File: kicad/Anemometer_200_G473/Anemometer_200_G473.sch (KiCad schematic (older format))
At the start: 81 parts, among them J1 Conn_01x01_Female, J10 Conn_01x01_Female, J11 USB_B_Micro, J12 Conn_01x01_Female, J13 Conn_01x01_Female, J14 Conn_01x01_Female, J15 Conn_01x01_Female, J16 Conn_01x01_Female, J17 Conn_01x01_Female, J18 Conn_01x01_Female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

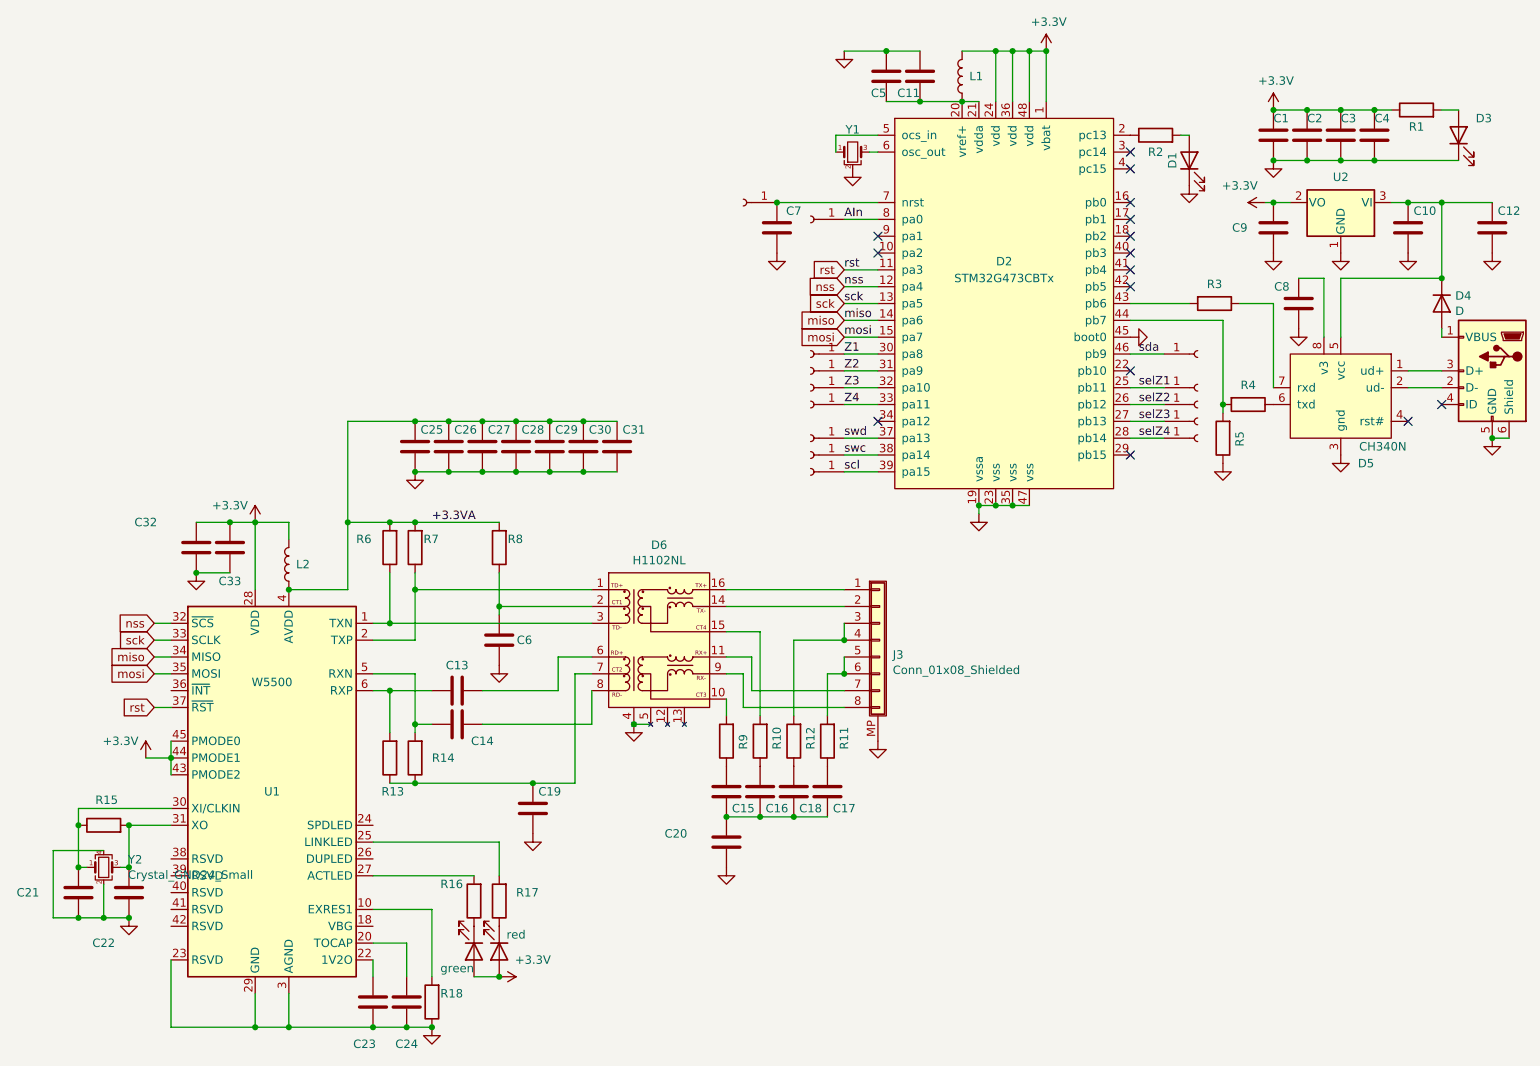
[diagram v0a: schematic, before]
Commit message: изменено:      kicad/Anemometer_200_G473/Anemometer_200_G473-cache.lib 	изменено:      kicad/Anemometer_200_G473/Anemometer_200_G473.kicad_pcb 	изменено:      kicad/Anemometer_200_G473/Anemometer_200_G473.kicad_pcb-bak 	изменено:      kicad/Anemometer_200_G473/Anemometer_200_G473.sch 	изменено:      kicad/Anemometer_200_G473/Anemometer_200_G473.sch-bak 	изменено:      kicad/Anemometer_200_G473/sym-lib-table 	изменено:      stm32cubeide/Anemometer_G474CBT6_MATLAB/Anemometer_G473CBT7_MATLAB.ioc 	изменено:      stm32cubeide/Anemometer_G474CBT6_MATLAB/Core/Inc/main.h 	изменено:      stm32cubeide/Anemometer_G474CBT6_MATLAB/Core/Src/main.c 	изменено:      stm32cubeide/Anemometer_G474CBT6_MATLAB/Release/Anemometer_G473CBT7_MATLAB.elf 	изменено:      stm32cubeide/Anemometer_G474CBT6_MATLAB/Release/Anemometer_G473CBT7_MATLAB.list 	изменено:      stm32cubeide/Anemometer_G474CBT6_MATLAB/Release/Anemometer_G473CBT7_MATLAB.map 	изменено:      stm32cubeide/Anemometer_G474CBT6_MATLAB/Release/Core/Src/main.cyclo 	изменено:      stm32cubeide/Anemometer_G474CBT6_MATLAB/Release/Core/Src/main.o 	изменено:      stm32cubeide/Anemometer_G474CBT6_MATLAB/Release/Core/Src/main.su
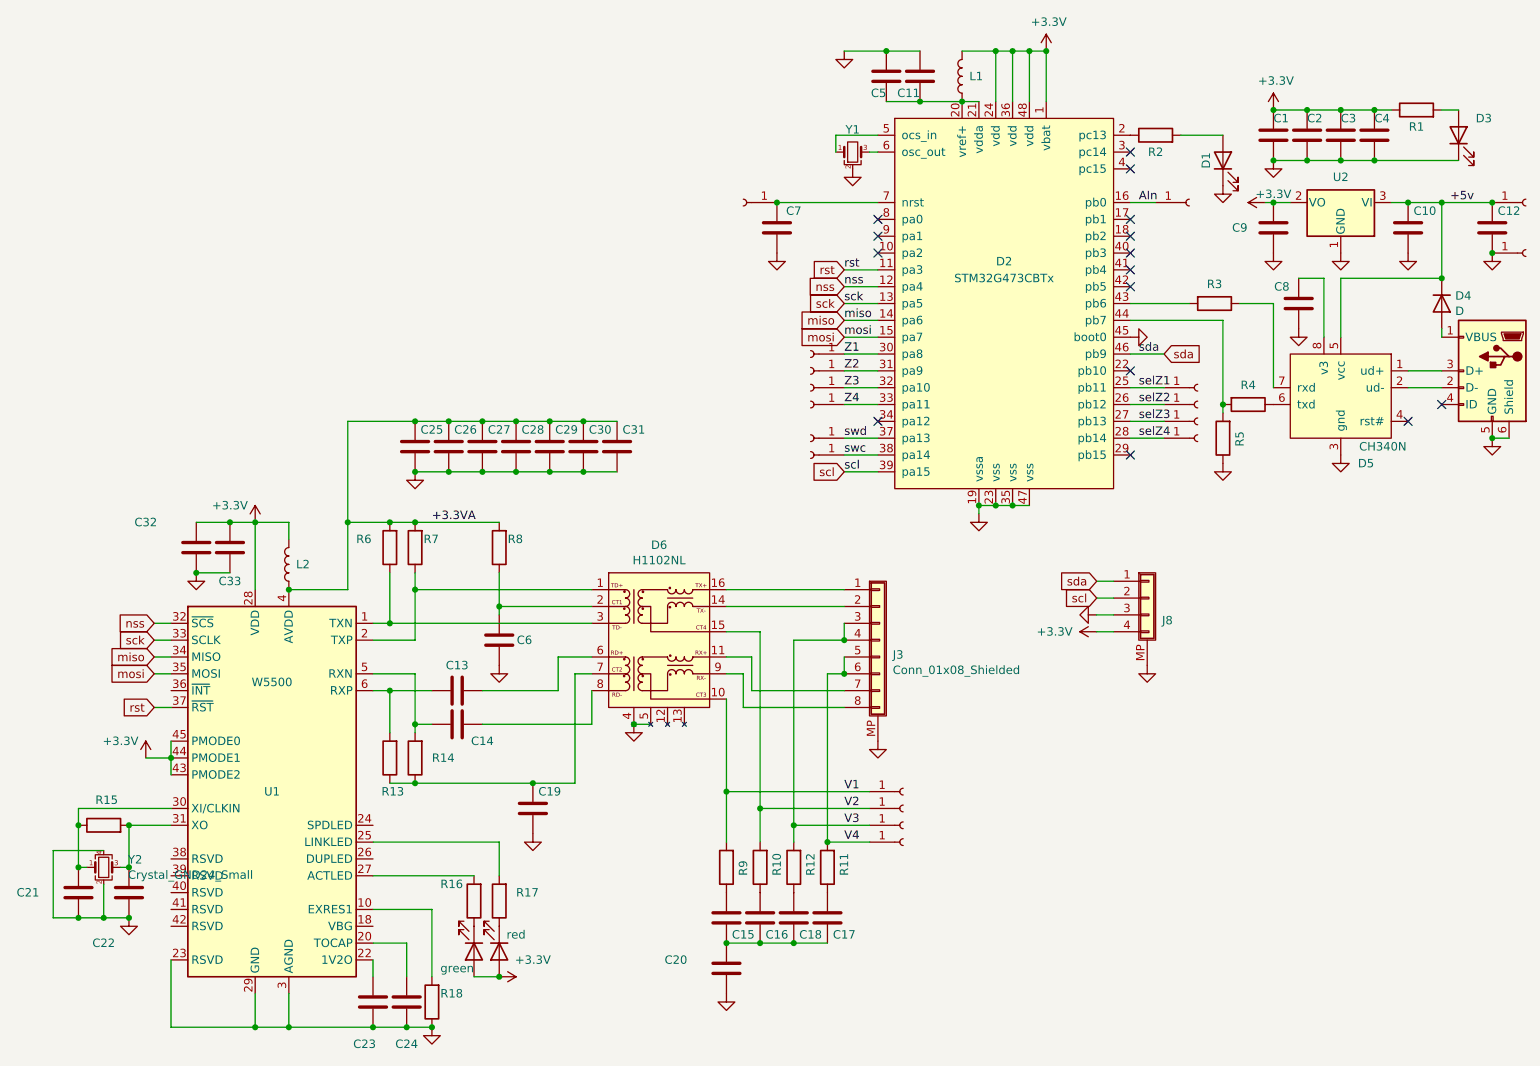
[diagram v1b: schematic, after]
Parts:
- removed J22: Conn_01x01_Female, My-library:mini_conn, symbol Connector:Conn_01x01_Female
- added J19, J4, J5, J6, J7: Conn_01x01_Female, My-library:mini_conn, symbol Connector:Conn_01x01_Female
- added J8: Conn_01x04_Shielded, Connector_JST:JST_SH_BM04B-SRSS-TB_1x04-1MP_P1.00mm_Vertical, symbol My_Library:Conn_01x04_Shielded
- C11, C33, C4, C5: footprint Capacitor_SMD:C_0603_1608Metric -> Capacitor_SMD:C_0805_2012Metric
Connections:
- net +3V3: now also J8.4 (Pin_4)
- net AIn: now also D2.16 (pb0); no longer D2.8 (pa0)
- net GND: now also J19.1 (Pin_1), J8.3 (Pin_3), J8.MP (Shield)
- net scl: now also J8.2 (Pin_2); no longer J18.1 (Pin_1)
- net sda: now also J8.1 (Pin_1)
- net +5v: now reaches C10.1, C12.1, D4.1 (K), D5.5 (vcc), U2.3 (VI)
- net +5v: now also J18.1 (Pin_1)
- net V1: now reaches D6.10, R9.2
- net V1: now also J4.1 (Pin_1)
- net V2: now reaches D6.15, R10.2
- net V2: now also J5.1 (Pin_1)
- net V4: now reaches J3.5 (Pin_5), J3.6 (Pin_6), R11.2
- net V4: now also J7.1 (Pin_1)
- net V3: now reaches J3.3 (Pin_3), J3.4 (Pin_4), R12.2
- net V3: now also J6.1 (Pin_1)
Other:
- moved on the sheet: C15, C16, C17, C18, C20, D1, R10, R11, R12, R9

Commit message: изменено:      kicad/Anemometer_200_G473/Anemometer_200_G473.sch 	изменено:      kicad/Anemometer_200_G473/Anemometer_200_G473.sch-bak 	изменено:      stm32cubeide/Anemometer_G474CBT6_MATLAB/.mxproject 	изменено:      stm32cubeide/Anemometer_G474CBT6_MATLAB/Anemometer_G473CBT7_MATLAB.ioc 	изменено:      stm32cubeide/Anemometer_G474CBT6_MATLAB/Core/Inc/main.h 	изменено:      stm32cubeide/Anemometer_G474CBT6_MATLAB/Core/Inc/stm32g4xx_hal_conf.h 	изменено:      stm32cubeide/Anemometer_G474CBT6_MATLAB/Core/Src/main.c 	изменено:      stm32cubeide/Anemometer_G474CBT6_MATLAB/Core/Src/stm32g4xx_hal_msp.c 	изменено:      stm32cubeide/Anemometer_G474CBT6_MATLAB/Core/Src/stm32g4xx_it.c 	изменено:      stm32cubeide/Anemometer_G474CBT6_MATLAB/Release/Anemometer_G473CBT7_MATLAB.elf 	изменено:      stm32cubeide/Anemometer_G474CBT6_MATLAB/Release/Anemometer_G473CBT7_MATLAB.list 	изменено:      stm32cubeide/Anemometer_G474CBT6_MATLAB/Release/Anemometer_G473CBT7_MATLAB.map 	изменено:      stm32cubeide/Anemometer_G474CBT6_MATLAB/Release/Core/Src/BME280.d 	изменено:      stm32cubeide/Anemometer_G474CBT6_MATLAB/Release/Core/Src/main.cyclo 	изменено:      stm32cubeide/Anemometer_G474CBT6_MATLAB/Release/Core/Src/main.d 	изменено:      stm32cubeide/Anemometer_G474CBT6_MATLAB/Release/Core/Src/main.o 	изменено:      stm32cubeide/Anemometer_G474CBT6_MATLAB/Release/Core/Src/main.su 	изменено:      stm32cubeide/Anemometer_G474CBT6_MATLAB/Release/Core/Src/stm32g4xx_hal_msp.cyclo 	изменено:      stm32cubeide/Anemometer_G474CBT6_MATLAB/Release/Core/Src/stm32g4xx_hal_msp.d 	изменено:      stm32cubeide/Anemometer_G474CBT6_MATLAB/Release/Core/Src/stm32g4xx_hal_msp.o 	изменено:      stm32cubeide/Anemometer_G474CBT6_MATLAB/Release/Core/Src/stm32g4xx_hal_msp.su 	изменено:      stm32cubeide/Anemometer_G474CBT6_MATLAB/Release/Core/Src/stm32g4xx_it.cyclo 	изменено:      stm32cubeide/Anemometer_G474CBT6_MATLAB/Release/Core/Src/stm32g4xx_it.d 	изменено:      stm32cubeide/Anemometer_G474CBT6_MATLAB/Release/Co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
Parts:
- C32: value 22n -> 10u
- C33: value 22n -> .1
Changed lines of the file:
@@
 P 2350 4050
 F 0 "C33" H 2350 3850 50  0000 C CNN
-F 1 "22n" H 2465 4005 50  0001 L CNN
+F 1 ".1" H 2465 4005 50  0001 L CNN
 F 2 "Capacitor_SMD:C_0805_2012Metric" H 2388 3900 50  0001 C CNN
 F 3 "~" H 2350 4050 50  0001 C CNN
@@
 P 2150 4050
 F 0 "C32" H 1850 4200 50  0000 C CNN
-F 1 "22n" H 2265 4005 50  0001 L CNN
+F 1 "10u" H 2265 4005 50  0001 L CNN
 F 2 "Capacitor_SMD:C_0402_1005Metric" H 2188 3900 50  0001 C CNN
 F 3 "~" H 2150 4050 50  0001 C CNN
